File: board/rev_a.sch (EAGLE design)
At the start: 12 parts, among them IC1 STM32-M-48, IC2 LM2936DT-5.0, IC3 MCP6004, Q1 35A/25V/8.5mΩ, U1 3.3V/150mA

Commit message: [board] Updated PCB and IOC files
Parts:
- added C1: 47pF, resistor:C-EUC0603
- added D2, D3: BAT54S, diode:BAT54S
- added IC4: 25LC040ST, microchip:25LC040ST
- added MCU: STM32-M-48, pel_stm32:STM32-M-48
- added OP1: MCP6004, linear:MCP604ST
- added Q2: 600mA/40V, SparkFun-DiscreteSemi:TRANS_PNP-MMBT4403
- added R3: 22K, resistor:R-EU_R0603
- added R4, R5: 1K, resistor:R-EU_R0603
- added RN1, RN2: 1K, resistor-dil:4R-N0603-ARC
- IC1: value STM32-M-48 -> TJA1027; device pel_stm32:STM32-M-48 -> misc:MCP2004
- IC3: value MCP6004 -> MCP2551; device linear:MCP604ST -> SparkFun-IC-Comms:MCP2551
- renumbered IC2 to LDO1, U1 to LDO2
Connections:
- net N$4 renamed HEATER_CTRL
- new net CAN_CSN: IC3.RS, R3.1
- new net CAN_RX: IC3.RXD, MCU.PB8-TIM4CH3-I2C1SCL/CANRX
- new net CAN_TX: IC3.TXD, MCU.PB9-TIM4CH4-I2C1SDA/CANTX
- new net KLINE: IC1.LBUS@6, R5.2
- new net KLINE_PULLUP: R4.1
- new net LED_B: RN1D.2
- new net LED_G: RN1B.2
- new net LED_R: RN1C.2
- new net N$1: Q2.C, R5.1
- new net N$10: OP1B.OUT
- new net N$11: OP1A.OUT
- new net N$3: D1.BLU-C, RN1D.1
- new net N$4: C1.1, LDO2.BP
- new net N$5: D1.GRN-C, RN1B.1
- new net N$6: D1.RED-C, RN1C.1
- new net N$7: Q2.B, R4.2
- new net OUT1: D2.C1A2, IC3.CANH, OP1C.OUT, RN2A.2, RN2B.2
- new net OUT1_C: J1.3, RN2A.1, RN2B.1
- new net OUT2: D3.C1A2, IC3.CANL, OP1D.OUT, RN2C.2, RN2D.2
- new net OUT2_C: J1.2, RN2C.1, RN2D.1
- new net SPI2_CLK: IC4.SCK, MCU.PB13-SPI2SCK/USART3CTS/TIM1CH1N
- new net SPI2_CS: IC4.!CS
- new net SPI2_MISO: IC4.SO, MCU.PB14-SPI2MISO/USART3RTS/TIM1CH2N
- new net SPI2_MOSI: IC4.SI, MCU.PB15-SPI2MOSI/TIM1CH3N
- new net USART_CS: IC1.CS/WAKE@2
- new net USART_RX: IC1.RXD@1
- new net USART_TX: IC1.TXD@4
- net 12V: now also IC1.VBB@7, Q2.E
- net 5V: now also D1.BLU-A, D1.RED-A, D2.C2, D3.C2, IC3.VDD, OP1P.V+; no longer IC3P.V+
- net GND: now also C1.2, D2.A1, D3.A1, IC1.VSS@5, IC3.VSS, IC4.!HOLD, IC4.!WP, IC4.GND, MCU.VSS1, MCU.VSS2, MCU.VSS3, OP1P.V-, R3.2; no longer IC1.VSS1, IC1.VSS2, IC1.VSS3, IC3P.V-
- net VBAT: now also MCU.VBAT; no longer IC1.VBAT
- net VCC: now also IC1.FAULT/TXE@3, IC4.VCC, MCU.VDD1, MCU.VDD2, MCU.VDD3, MCU.VDDA; no longer IC1.VDD1, IC1.VDD2, IC1.VDD3, IC1.VDDA
- net VSSA: now also MCU.VSSA; no longer IC1.VSSA

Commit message: [board] Cleaning up
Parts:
- removed IC1: TJA1027, misc:MCP2004
- removed IC4: 25LC040ST, microchip:25LC040ST
- removed Q2: 600mA/40V, SparkFun-DiscreteSemi:TRANS_PNP-MMBT4403
- removed R1, R4, R5: 1K, resistor:R-EU_R0603
- removed R2: 10K, resistor:R-EU_R0603
- added RN3: 1K, resistor-dil:4R-N0603-ARC
- added S1: (no value), SparkFun-Switches:MOMENTARY-SWITCH-SPST-2-SMD-5.2MM
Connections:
- net CAN_CSN renamed N$8
- removed net KLINE: IC1.LBUS@6, R5.2
- removed net KLINE_PULLUP: R4.1
- removed net LED_B: RN1D.2
- removed net LED_G: RN1B.2
- removed net LED_R: RN1C.2
- removed net OUT1_C: J1.3, RN2A.1, RN2B.1
- removed net OUT2_C: J1.2, RN2C.1, RN2D.1
- removed net SPI2_CLK: IC4.SCK, MCU.PB13-SPI2SCK/USART3CTS/TIM1CH1N
- removed net SPI2_CS: IC4.!CS
- removed net SPI2_MISO: IC4.SO, MCU.PB14-SPI2MISO/USART3RTS/TIM1CH2N
- removed net SPI2_MOSI: IC4.SI, MCU.PB15-SPI2MOSI/TIM1CH3N
- removed net USART_CS: IC1.CS/WAKE@2
- removed net USART_RX: IC1.RXD@1
- removed net USART_TX: IC1.TXD@4
- new net AN1: MCU.PA0-WKUP/USART2CTS/ADC0/TIM2CH1ETR
- new net AN2: MCU.PA6-SPI1MISO/ADC6/TIM3CH1-TIM1BKIN
- new net AN3: MCU.PA7-SPI1MOSI/ADC7/TIM3CH2-TIM1CH1N
- new net BUTTON1: MCU.PC13-TAMPER-RTC, S1.1, S1.2
- new net CAN_RS: MCU.PC14-OSC32_IN, R3.2
- new net DAC1: MCU.PA4-SPI1NSS/ADC4/USART2CK
- new net DAC2: MCU.PA5-SPI1SCK/ADC5
- new net NRST: MCU.NRST
- new net OPA1_IN+: MCU.PA1-USART2RTS/ADC1/TIM2CH2
- new net OPA1_IN-: MCU.PA3-USART2RX/ADC3/TIM2CH4
- new net OPA1_OUT: MCU.PA2-USART2TX/ADC2/TIM2CH3
- new net OPA3_IN+: MCU.PB0-ADC8/TIM3CH3-TIM1CH2N
- new net OPA3_IN-: MCU.PB2/BOOT1
- new net OPA3_OUT: MCU.PB1-ADC9/TIM3CH4-TIM1CH3N
- new net OPA4_IN+: MCU.PB11-I2C2SDA/USART3RX-TIM2CH4
- new net OPA4_IN-: MCU.PB10-I2C2SCL/USART3TX-TIM2CH3
- new net OPA4_OUT: MCU.PB12-SPI2NSS/I2C2SMBAI/USART3CK/TIM1BKIN
- new net OUT1_PROT: D2.C1A2, MCU.PA9-USART1TX/TIM1CH2, OP1C.OUT, RN2A.2, RN2B.2
- new net OUT2_PROT: D3.C1A2, MCU.PA10-USART1RX/TIM1CH3, OP1D.OUT, RN2C.2, RN2D.2
- new net SWDCLK: MCU.PA14/JTCK/SWCLK
- new net SWDIO: MCU.PA13/JTMS/SWDIO
- new net TIM2_CH2: MCU.PB15-SPI2MOSI/TIM1CH3N
- new net TIM4_CH1: MCU.PB6-I2C1SCL/TIM4CH1-USART1TX, RN1D.2
- new net TIM4_CH2: MCU.PB7-I2C1SDA/TIM4CH2-USART1RX, RN1B.2
- new net TIM4_CH3: MCU.PB8-TIM4CH3-I2C1SCL/CANRX, RN1C.2
- new net TIM4_CH4: MCU.PB9-TIM4CH4-I2C1SDA/CANTX
- net 12V: no longer IC1.VBB@7, Q2.E
- net 5V: now also D1.GRN-A
- net CAN_RX: now also MCU.PA11-USART1CTS/CANRX/USBDM/TIM1CH4; no longer MCU.PB8-TIM4CH3-I2C1SCL/CANRX
- net CAN_TX: now also MCU.PA12-USART1RTS/CANTX/USBDP/TIM1ETR; no longer MCU.PB9-TIM4CH4-I2C1SDA/CANTX
- net GND: now also RN3D.2, S1.3, S1.4; no longer IC1.VSS@5, IC4.!HOLD, IC4.!WP, IC4.GND, R2.1, R3.2
- net HEATER_CTRL: now also MCU.PB14-SPI2MISO/USART3RTS/TIM1CH2N, RN3A.1, RN3B.1; no longer R1.1, R2.2
- net N$1: now also Q1.G, RN3A.2; no longer Q2.C, R5.1
- net N$2: now also RN3B.2, RN3C.1; no longer Q1.G, R1.2
- net N$7: now also RN3C.2, RN3D.1; no longer Q2.B, R4.2
- net OUT1: now also J1.3, RN2A.1, RN2B.1; no longer D2.C1A2, OP1C.OUT, RN2A.2, RN2B.2
- net OUT2: now also J1.2, RN2C.1, RN2D.1; no longer D3.C1A2, OP1D.OUT, RN2C.2, RN2D.2
- net VCC: now also MCU.BOOT0; no longer IC1.FAULT/TXE@3, IC4.VCC
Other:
- moved on the sheet: Q1, R3

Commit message: [board] Testing a few configurations
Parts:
- removed OP1: MCP6004, linear:MCP604ST
- added C4, C5, C6: 100nF, resistor:C-EUC0603
- added D4: BAT54S, diode:BAT54S
- added J3: (no value), SparkFun-Connectors:CONN_04LOCK
- added LDO3: 3.3V/150mA, SparkFun-IC-Power:V_REG_MIC52053.3V
- added OPA5: MCP602ST, linear:MCP602ST
- added R1, R4: 20K, resistor:R-EU_R0603
- added R2, R5: 10K, resistor:R-EU_R0603
- added R6: 330K, resistor:R-EU_R0603
- added R7: 22K, resistor:R-EU_R0603
- added RN4: 1K, resistor-dil:4R-N0603-ARC
- D1: value (none) -> BAT54S; device SparkFun-LED:LED-RGBNO_IC -> diode:BAT54S
- J1: device SparkFun-Connectors:CONN_04LOCK_LONGPADS -> SparkFun-Connectors:CONN_06LONGPADS
- LDO1: value LM2936DT-5.0 -> LM2931DT-5.0
- MCU: value STM32-M-48 -> STM32F303CB
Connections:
- removed net N$4: C1.1, LDO2.BP
- removed net TIM4_CH1: MCU.PB6-I2C1SCL/TIM4CH1-USART1TX, RN1D.2
- removed net TIM4_CH2: MCU.PB7-I2C1SDA/TIM4CH2-USART1RX, RN1B.2
- new net N$9: RN1C.2, RN1D.1
- new net OUT3: IC3.CANH, J1.3, RN4A.1, RN4B.1
- new net OUT3_PROT: D1.C1A2, MCU.PA9-USART1TX/TIM1CH2, RN4A.2, RN4B.2
- new net OUT4: IC3.CANL, J1.2, RN4C.1, RN4D.1
- new net OUT4_PROT: D4.C1A2, MCU.PA10-USART1RX/TIM1CH3, RN4C.2, RN4D.2
- new net SCL: J3.3, MCU.PB6-I2C1SCL/TIM4CH1-USART1TX, RN1C.1
- new net SDA: J3.4, MCU.PB7-I2C1SDA/TIM4CH2-USART1RX, RN1A.1
- new net VDDA: C6.1, LDO3.OUT, MCU.VDDA
- net 12V: now also J1.6; no longer J1.4
- net 5V: now also C5.1, D1.C2, D4.C2, J3.2, LDO3.EN, LDO3.IN, OPA5P.V+, RN1B.2, RN1D.2; no longer D1.BLU-A, D1.GRN-A, D1.RED-A, OP1P.V+
- net BUTTON1: now also C4.1
- net DAC1: now also OPA5A.+IN
- net DAC2: now also OPA5B.+IN
- net GND: now also C4.2, C5.2, C6.2, D1.A1, D4.A1, J3.1, LDO3.GND, MCU.BOOT0, OPA5P.V-, R1.1, R4.1; no longer OP1P.V-
- net IP: now also R7.1
- net N$10: now also R6.1, R7.2; no longer OP1B.OUT
- net N$11: now also C1.1, LDO3.BP; no longer OP1A.OUT
- net N$3: now also RN1A.2, RN1B.1; no longer D1.BLU-C, RN1D.1
- net N$5: now also OPA5A.-IN, R1.2, R2.2; no longer D1.GRN-C, RN1B.1
- net N$6: now also R4.2, R5.2; no longer D1.RED-C, RN1C.1
- net OPA3_OUT: now also R6.2
- net OUT1: now also J1.5; no longer IC3.CANH, J1.3
- net OUT1_PROT: now also OPA5A.OUT, R2.1; no longer MCU.PA9-USART1TX/TIM1CH2, OP1C.OUT
- net OUT2: now also J1.4; no longer IC3.CANL, J1.2
- net OUT2_PROT: now also OPA5B.OUT, R5.1; no longer MCU.PA10-USART1RX/TIM1CH3, OP1D.OUT
- net TIM4_CH3: no longer RN1C.2
- net VCC: no longer MCU.BOOT0, MCU.VDDA
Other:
- note added: "OPA3"
- note added: "Pump cell current"
- moved on the sheet: C1, C3, D2, D3, IC3, J2, LDO1, R3, RN1B, RN1C, RN1D, RN2A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

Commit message: [board] Working on schema
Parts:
- added C8, C9: 100nF, resistor:C-EUC0603
- added D5: BAT54S, diode:BAT54S
- added IC1: MCP604ST, linear:MCP604ST
- added R11, R12: 10K, resistor:R-EU_R0603
- added R8: 20K 1%, resistor:R-EU_R0603
- added R9: 1K 1%, resistor:R-EU_R0603
- added X1: B4B-ZR, con-jst:B4B-ZR
- C1: value 47pF -> 100nF
- LDO1: value LM2931DT-5.0 -> LM2931-5.0
- LDO2, LDO3: value 3.3V/150mA -> LDK120DM33R
- Q1: value 35A/25V/8.5mΩ -> Logic level FET
- R1, R4: value 20K -> 20K 1%
- R2, R5: value 10K -> 10K 1%
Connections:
- net HEATER_CTRL renamed TIM15_CH1
- net TIM2_CH2 renamed TIM15_CH2
- removed net SWDCLK: MCU.PA14/JTCK/SWCLK
- new net N$13: C9.1, OPA5A.+IN, R12.2
- new net N$4: C8.1, OPA5B.+IN, R11.2
- new net PUMP_DRV: IC1A.-IN, IC1A.OUT
- new net PUMP_REF: IC1B.-IN, IC1B.OUT
- new net SWCLK: MCU.PA14/JTCK/SWCLK, X1-1.1
- net 12V: now also R8.1
- net 5V: no longer RN1B.2, RN1D.2
- net AN3: now also D5.C1A2, R8.2, R9.2
- net BUTTON1: no longer C4.1
- net DAC1: now also IC1A.+IN; no longer OPA5A.+IN
- net DAC2: now also IC1B.+IN; no longer OPA5B.+IN
- net GND: now also C8.2, C9.2, D5.A1, IC1P.V-, R9.1, X1-2.1
- net N$6: now also OPA5B.-IN
- net NRST: now also C4.1, X1-4.1
- net OPA1_OUT: now also R6.2
- net OPA3_OUT: no longer R6.2
- net SWDIO: now also X1-3.1
- net TIM4_CH3: now also R12.1
- net TIM4_CH4: now also R11.1
- net VCC: now also RN1B.2, RN1D.2
- net VDDA: now also D5.C2, IC1P.V+
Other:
- note added: "OPA1"
- note added: "VBAT monitoring"
- note removed: "OPA3"
- moved on the sheet: C4, R1, R2, R4, R5

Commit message: [board] Adding a few analog circuits
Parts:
- removed IC1: MCP604ST, linear:MCP604ST
- added C7: 100nF, resistor:C-EUC0603
- added OPA1: MCP6002, linear:MCP602ST
- added R10: 22K 1%, resistor:R-EU_R0603
- added R13: 100K 1%, resistor:R-EU_R0603
- added R14: 61.9R 1%, resistor:R-EU_R0603
- added R15: 10K 1%, resistor:R-EU_R0603
- added R16: 150K 1%, resistor:R-EU_R0603
- C8, C9: value 100nF -> 10nF
- OPA2: value MCP602ST -> MCP6002
- R11, R12: value 10K -> 10K 1%
- R6: value 330K -> 100K 1%
- R7: value 22K -> 22K 1%
- renumbered OPA5 to OPA2
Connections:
- net OPA4_IN+ renamed VS/OPA4_IN+
- removed net CAL_RES: J2.5
- removed net N$10: R6.1, R7.2
- removed net OPA1_IN+: MCU.PA1-USART2RTS/ADC1/TIM2CH2
- removed net OPA1_IN-: MCU.PA3-USART2RX/ADC3/TIM2CH4
- removed net OPA1_OUT: MCU.PA2-USART2TX/ADC2/TIM2CH3, R6.2
- removed net PUMP_DRV: IC1A.-IN, IC1A.OUT
- removed net PUMP_REF: IC1B.-IN, IC1B.OUT
- removed net TIM15_CH2: MCU.PB15-SPI2MOSI/TIM1CH3N
- removed net VS/IP: J2.2
- new net N$12: C7.1, R15.1
- new net RCAL: J2.5, R10.1, R14.2
- new net TIM1_CH1: MCU.PA8-USART1CK/MCO/TIM1CH1, R15.2
- new net VS/IP_REF: J2.2, OPA1B.-IN, OPA1B.OUT, R13.2
- net AN1: now also D5.C1A2, R8.2, R9.2
- net AN2: now also MCU.PA1-USART2RTS/ADC1/TIM2CH2; no longer MCU.PA6-SPI1MISO/ADC6/TIM3CH1-TIM1BKIN
- net AN3: now also MCU.PA2-USART2TX/ADC2/TIM2CH3; no longer D5.C1A2, MCU.PA7-SPI1MOSI/ADC7/TIM3CH2-TIM1CH1N, R8.2, R9.2
- net DAC1: now also OPA1A.+IN; no longer IC1A.+IN
- net DAC2: now also OPA1B.+IN; no longer IC1B.+IN
- net GND: now also OPA1P.V-; no longer IC1P.V-
- net IP: now also OPA1A.-IN, OPA1A.OUT, R14.1
- net N$1: now also RN3B.1
- net OPA3_IN+: now also R10.2, R13.1
- net OPA3_IN-: now also R6.1, R7.2
- net OPA3_OUT: now also R6.2
- net TIM15_CH1: no longer RN3B.1
- net VDDA: now also OPA1P.V+; no longer IC1P.V+
- net VS: now also C7.2
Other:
- note added: "+"
- note added: "-"
- note added: "ADC3_1"
- note added: "ADC4_3"
- note added: "LSU 4.9 reference current"
- note added: "Nerst pulse"
- note added: "Nerst resistance PGA"
- note added: "OPA3"
- note added: "OPA4"
- note added: "Output PWM DACs - 16Mhz"
- note added: "Pump Drive Buffer"
- note added: "Read current across R14 Amplify by 5.5"
- note added: "VREF Buffer"
- note removed: "OPA1"
- moved on the sheet: R7

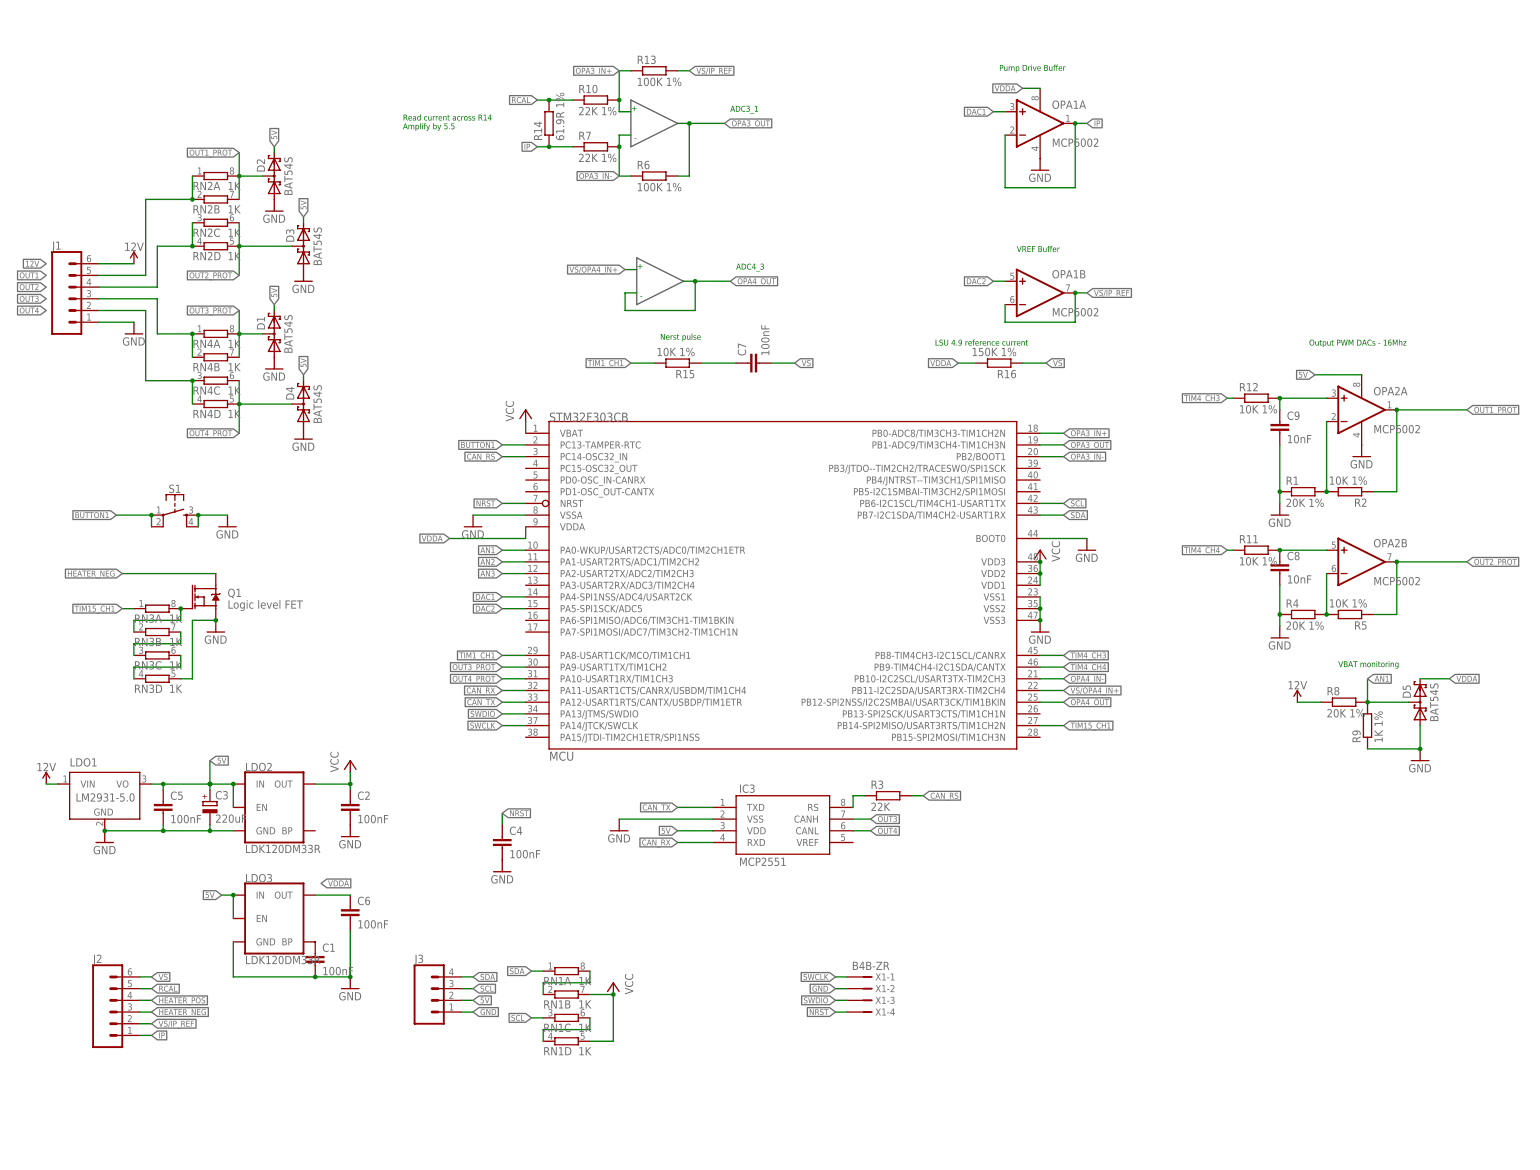
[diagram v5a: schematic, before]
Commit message: [board] Replacing diodes with smaller packages
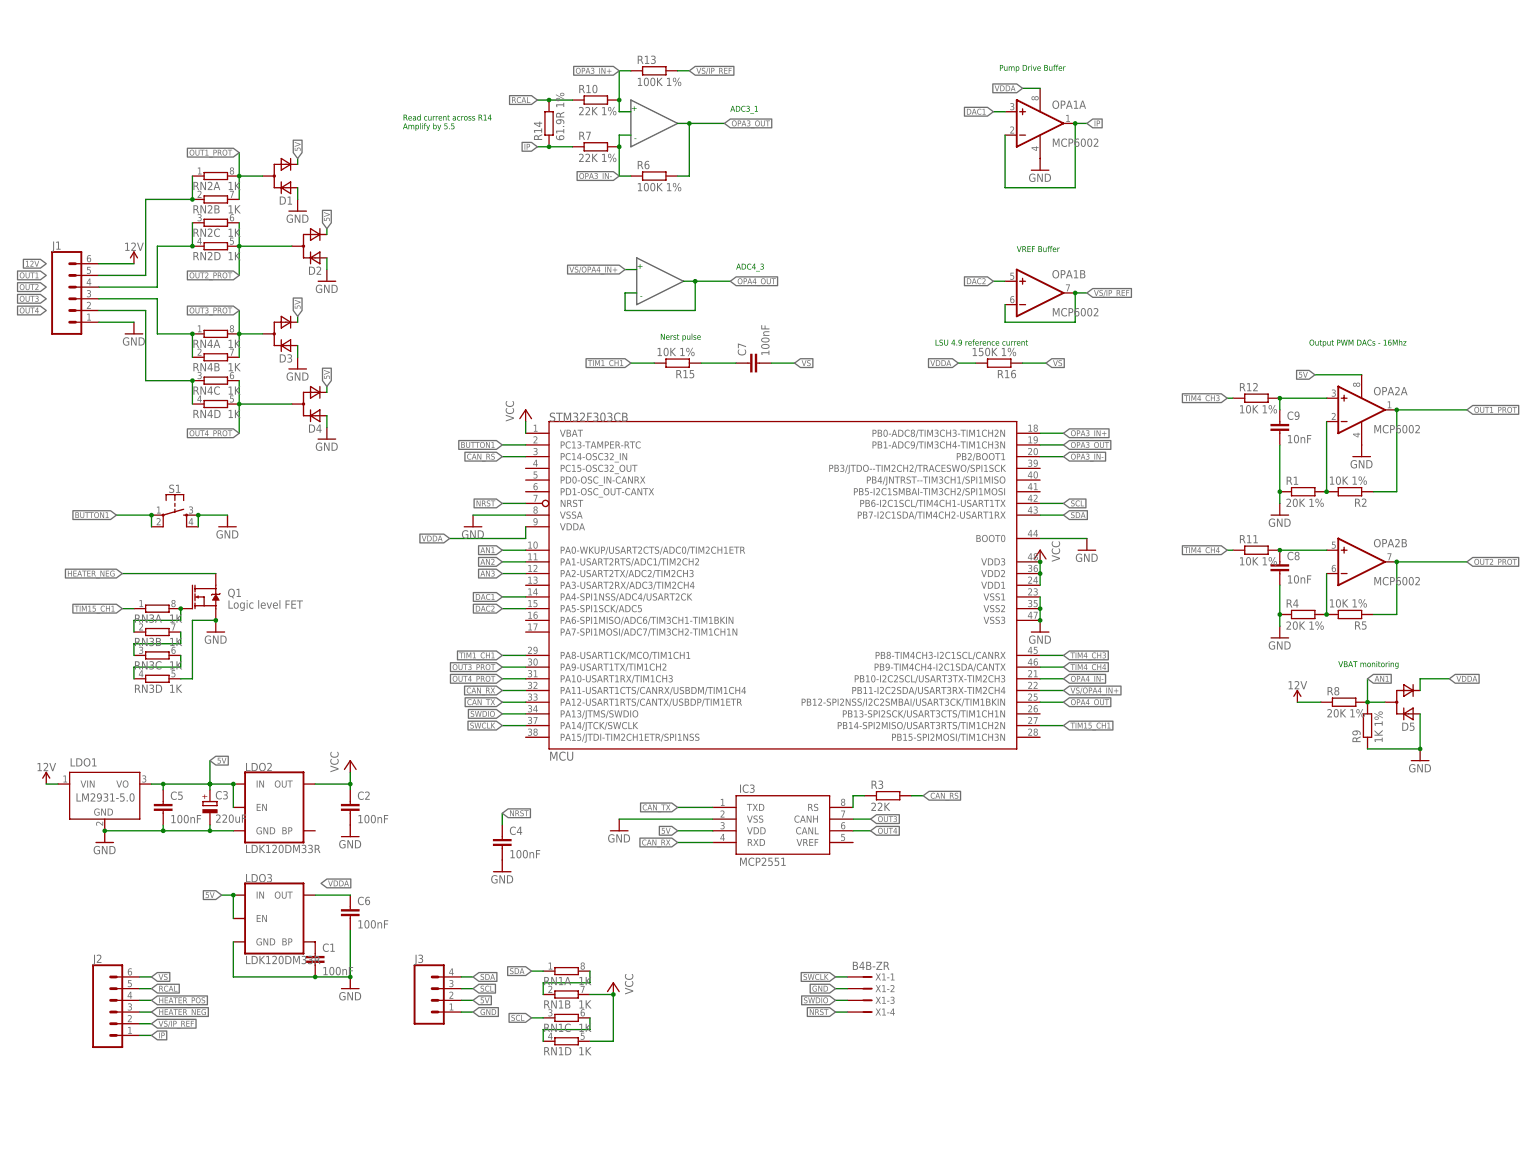
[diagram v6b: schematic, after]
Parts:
- D1, D2, D3, D4, D5: value BAT54S -> (none); device diode:BAT54S -> zetex:D_ACACSOT323
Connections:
- net 5V: now also D1.C, D2.C, D3.C, D4.C; no longer D1.C2, D2.C2, D3.C2, D4.C2
- net AN1: now also D5.CA; no longer D5.C1A2
- net GND: now also D1.A, D2.A, D3.A, D4.A, D5.A; no longer D1.A1, D2.A1, D3.A1, D4.A1, D5.A1
- net OUT1_PROT: now also D1.CA; no longer D2.C1A2
- net OUT2_PROT: now also D2.CA; no longer D3.C1A2
- net OUT3_PROT: now also D3.CA; no longer D1.C1A2
- net OUT4_PROT: now also D4.CA; no longer D4.C1A2
- net VDDA: now also D5.C; no longer D5.C2

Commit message: [board] Working on analog
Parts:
- added R17, R20: 66K 1%, resistor:R-EU_R0603
- added R18, R19: 22K 1%, resistor:R-EU_R0603
- added R21: 100R, resistor:R-EU_R0603
- R14: value 61.9R 1% -> 62R 1%
- R16: value 150K 1% -> 100K 1%
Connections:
- net CAN_RS renamed CAN_SLEEP
- removed net VS/IP_REF: J2.2, OPA1B.-IN, OPA1B.OUT, R13.2
- removed net VS/OPA4_IN+: MCU.PB11-I2C2SDA/USART3RX-TIM2CH4
- new net N$15: OPA1A.-IN, OPA1A.OUT, R21.2
- new net OPA4_IN+: MCU.PB11-I2C2SDA/USART3RX-TIM2CH4, R19.2, R20.1
- new net VGND: J2.2, OPA1B.-IN, OPA1B.OUT, R13.2, R18.1
- net GND: now also R20.2
- net IP: no longer OPA1A.-IN, OPA1A.OUT
- net OPA4_IN-: now also R17.1, R18.2
- net OPA4_OUT: now also R17.2
- net RCAL: now also R21.1
- net VDDA: now also R16.2
- net VS: now also R16.1, R19.1
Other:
- note added: "LSU 4.9 reference current (33 uA)"
- note added: "Nerst resistance"
- note added: "VBAT monitoring (Engine ON/OFF detection, heater current calculation)"
- note added: "VGND Buffer"
- note removed: "LSU 4.9 reference current"
- note removed: "Nerst resistance PGA"
- note removed: "VBAT monitoring"
- note removed: "VREF Buffer"
- moved on the sheet: C7, R15, R16
